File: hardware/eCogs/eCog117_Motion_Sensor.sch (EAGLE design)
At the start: 2 parts

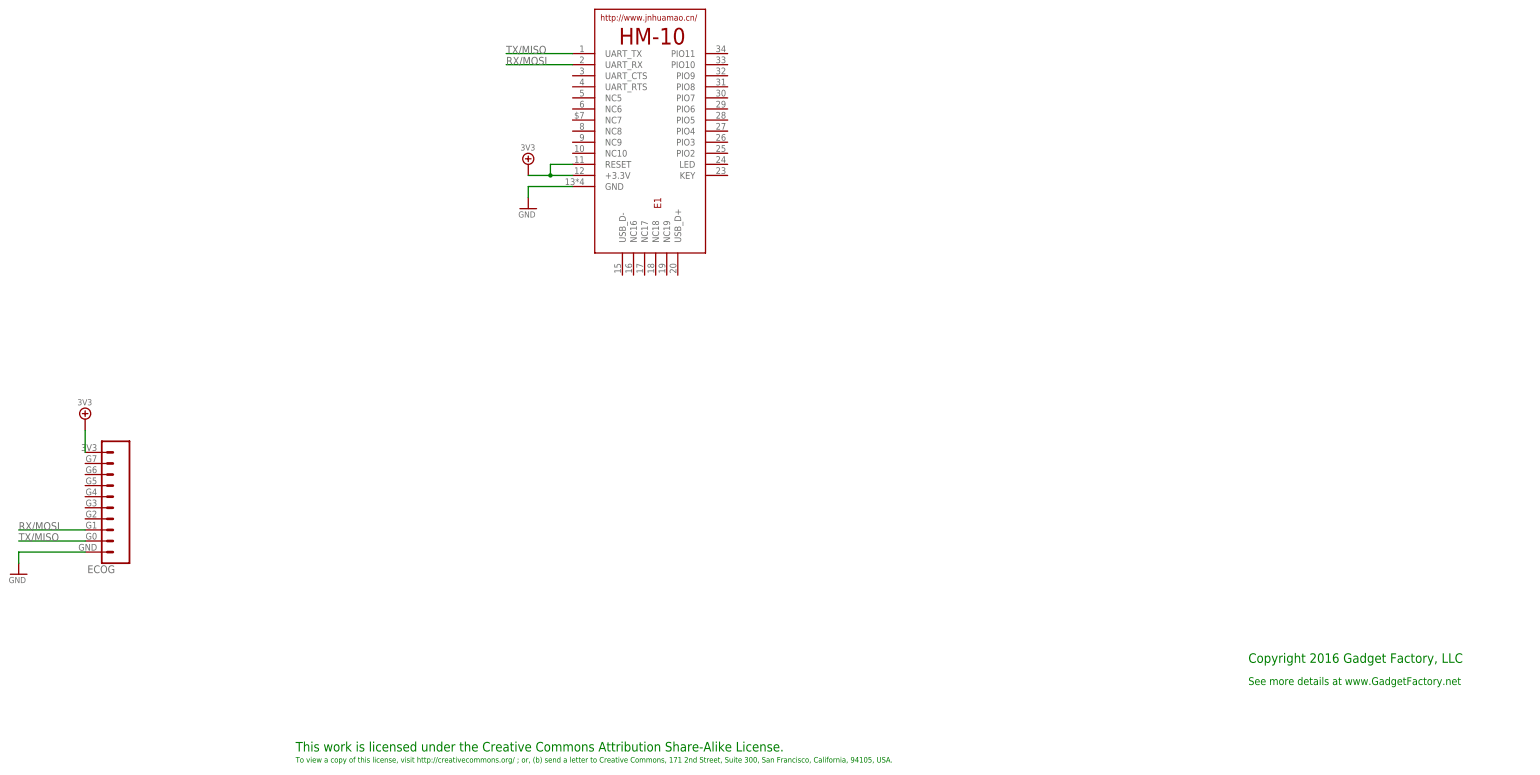
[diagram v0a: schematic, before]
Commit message: Update eCogs to through hole
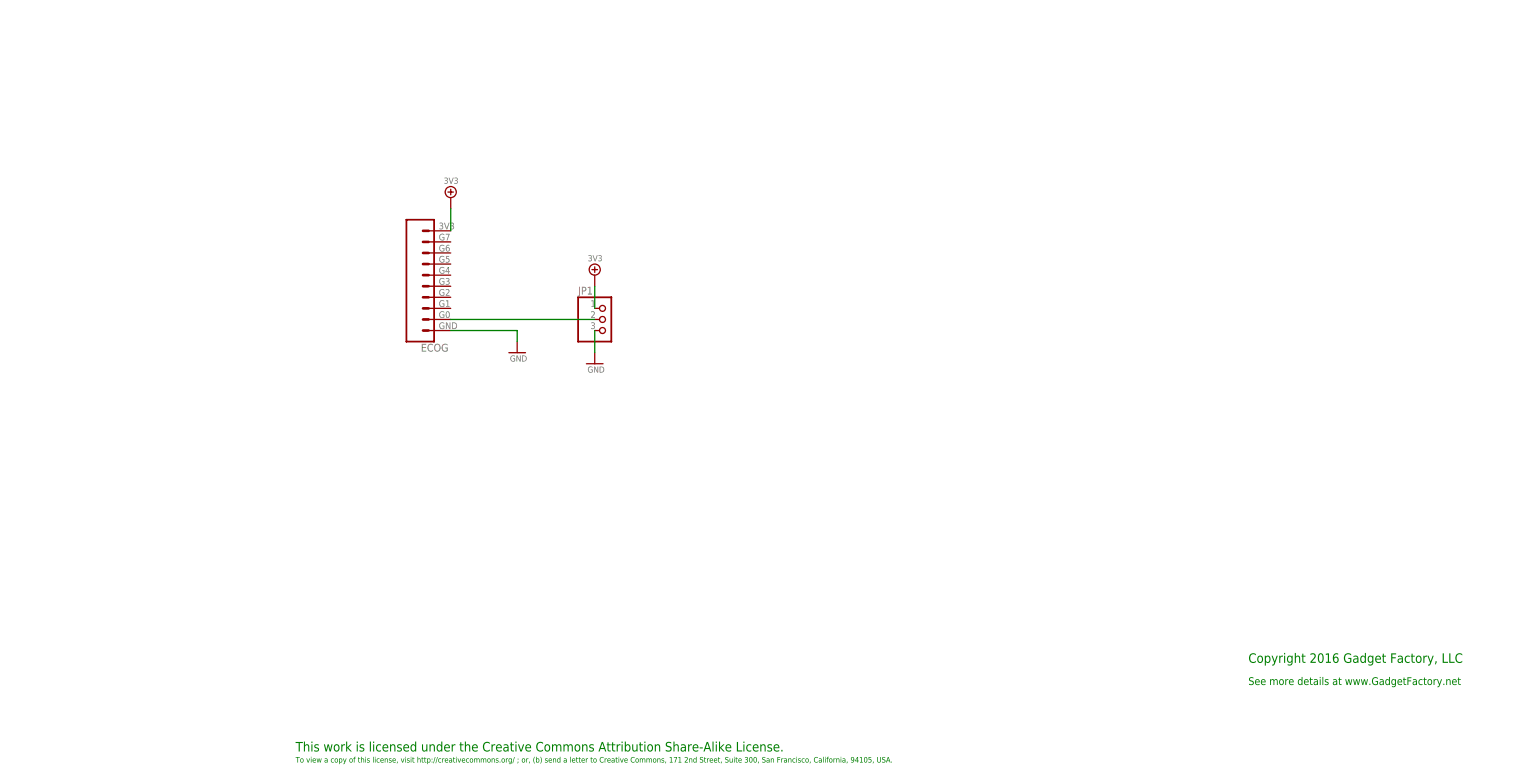
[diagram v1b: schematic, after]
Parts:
- removed E1: HM-10-BOARD, JNHuaMao:HM-10-BOARD
- added JP1: (no value), pinhead:PINHD-1X3
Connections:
- removed net RX/MOSI: E1.UART_RX, ECOG.G1
- removed net TX/MISO: E1.UART_TX, ECOG.G0
- new net N$1: ECOG.G0, JP1.2
- net 3V3: now also JP1.1; no longer E1.+3.3V, E1.RESET
- net GND: now also JP1.3; no longer E1.GND
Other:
- moved on the sheet: ECOG
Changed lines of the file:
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@@
 <part name="3V3_PWR1" library="eCogs" deviceset="3V3" device=""/>
 <part name="GND1" library="eCogs" deviceset="GND" device=""/>
-<part name="E1" library="JNHuaMao" deviceset="HM-10" device="-BOARD"/>
+<part name="JP1" library="pinhead" deviceset="PINHD-1X3" device=""/>
 <part name="3V3_PWR2" library="eCogs" deviceset="3V3" device=""/>
 <part name="GND2" library="eCogs" deviceset="GND" device=""/>
@@
 <instances>
 <instance part="FRAME1" gate="G$1" x="0" y="0"/>
-<instance part="ECOG" gate="ECOG_GENERAL" x="55.88" y="53.34"/>
-<instance part="3V3_PWR1" gate="A" x="50.8" y="86.36"/>
-<instance part="GND1" gate="A" x="35.56" y="50.8"/>
-<instance part="E1" gate="G$1" x="167.64" y="180.34"/>
-<instance part="3V3_PWR2" gate="A" x="152.4" y="144.78"/>
-<instance part="GND2" gate="A" x="152.4" y="134.62"/>
+<instance part="ECOG" gate="ECOG_GENERAL" x="129.54" y="104.14" rot="MR0"/>
+<instance part="3V3_PWR1" gate="A" x="134.62" y="137.16" rot="MR0"/>
+<instance part="GND1" gate="A" x="149.86" y="101.6" rot="MR0"/>
+<instance part="JP1" gate="A" x="170.18" y="109.22"/>
+<instance part="3V3_PWR2" gate="A" x="167.64" y="119.38" rot="MR0"/>
+<instance part="GND2" gate="A" x="167.64" y="99.06" rot="MR0"/>
 </instances>
 <busses>
@@
 <pinref part="ECOG" gate="ECOG_GENERAL" pin="3V3"/>
 <pinref part="3V3_PWR1" gate="A" pin="3V3"/>
-<wire x1="50.8" y1="78.74" x2="50.8" y2="83.82" width="0.2032" layer="91"/>
+<wire x1="134.62" y1="129.54" x2="134.62" y2="134.62" width="0.2032" layer="91"/>
 </segment>
 <segment>
+<pinref part="JP1" gate="A" pin="1"/>
 <pinref part="3V3_PWR2" gate="A" pin="3V3"/>
-<pinref part="E1" gate="G$1" pin="+3.3V"/>
-<wire x1="152.4" y1="142.24" x2="157.48" y2="142.24" width="0.2032" layer="91"/>
-<pinref part="E1" gate="G$1" pin="RESET"/>
-<wire x1="157.48" y1="142.24" x2="162.56" y2="142.24" width="0.2032" layer="91"/>
-<wire x1="162.56" y1="144.78" x2="157.48" y2="144.78" width="0.2032" layer="91"/>
-<wire x1="157.48" y1="144.78" x2="157.48" y2="142.24" width="0.2032" layer="91"/>
-<junction x="157.48" y="142.24"/>
+<wire x1="167.64" y1="116.84" x2="167.64" y2="111.76" width="0.1524" layer="91"/>
 </segment>
 </net>
@@
 <pinref part="ECOG" gate="ECOG_GENERAL" pin="GND"/>
 <pinref part="GND1" gate="A" pin="GND"/>
-<wire x1="50.8" y1="55.88" x2="35.56" y2="55.88" width="0.2032" layer="91"/>
-<wire x1="35.56" y1="55.88" x2="35.56" y2="53.34" width="0.2032" layer="91"/>
+<wire x1="134.62" y1="106.68" x2="149.86" y2="106.68" width="0.2032" layer="91"/>
+<wire x1="149.86" y1="106.68" x2="149.86" y2="104.14" width="0.2032" layer="91"/>
 </segment>
 <segment>
+<pinref part="JP1" gate="A" pin="3"/>
 <pinref part="GND2" gate="A" pin="GND"/>
-<wire x1="152.4" y1="137.16" x2="152.4" y2="139.7" width="0.2032" layer="91"/>
-<pinref part="E1" gate="G$1" pin="GND"/>
-<wire x1="152.4" y1="139.7" x2="162.56" y2="139.7" width="0.2032" layer="91"/>
+<wire x1="167.64" y1="101.6" x2="167.64" y2="106.68" width="0.1524" layer="91"/>
 </segment>
 </net>
-<net name="RX/MOSI" class="0">
+<net name="N$1" class="0">
 <segment>
-<pinref part="E1" gate="G$1" pin="UART_RX"/>
-<wire x1="162.56" y1="167.64" x2="147.32" y2="167.64" width="0.2032" layer="91"/>
-<label x="147.32" y="167.64" size="1.778" layer="95"/>
-</segment>
-<segment>
-<pinref part="ECOG" gate="ECOG_GENERAL" pin="G1"/>
-<wire x1="50.8" y1="60.96" x2="35.56" y2="60.96" width="0.2032" layer="91"/>
-<label x="35.56" y="60.96" size="1.778" layer="95"/>
+<pinref part="ECOG" gate="ECOG_GENERAL" pin="G0"/>
+<pinref part="JP1" gate="A" pin="2"/>
+<wire x1="134.62" y1="109.22" x2="167.64" y2="109.22" width="0.2032" layer="91"/>
 </segment>
 </net>
-<net name="TX/MISO" class="0">
-<segment>
-<pinref part="E1" gate="G$1" pin="UART_TX"/>
-<wire x1="162.56" y1="170.18" x2="147.32" y2="170.18" width="0.2032" layer="91"/>
-<label x="147.32" y="170.18" size="1.778" layer="95"/>
-</segment>
-<segment>
-<pinref part="ECOG" gate="ECOG_GENERAL" pin="G0"/>
-<wire x1="50.8" y1="58.42" x2="35.56" y2="58.42" width="0.2032" layer="91"/>
-<label x="35.56" y="58.42" size="1.778" layer="95"/>
-</segment>
-</net>
